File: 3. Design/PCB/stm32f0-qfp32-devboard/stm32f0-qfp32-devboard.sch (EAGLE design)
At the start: 11 parts, among them IC1 STM32F051

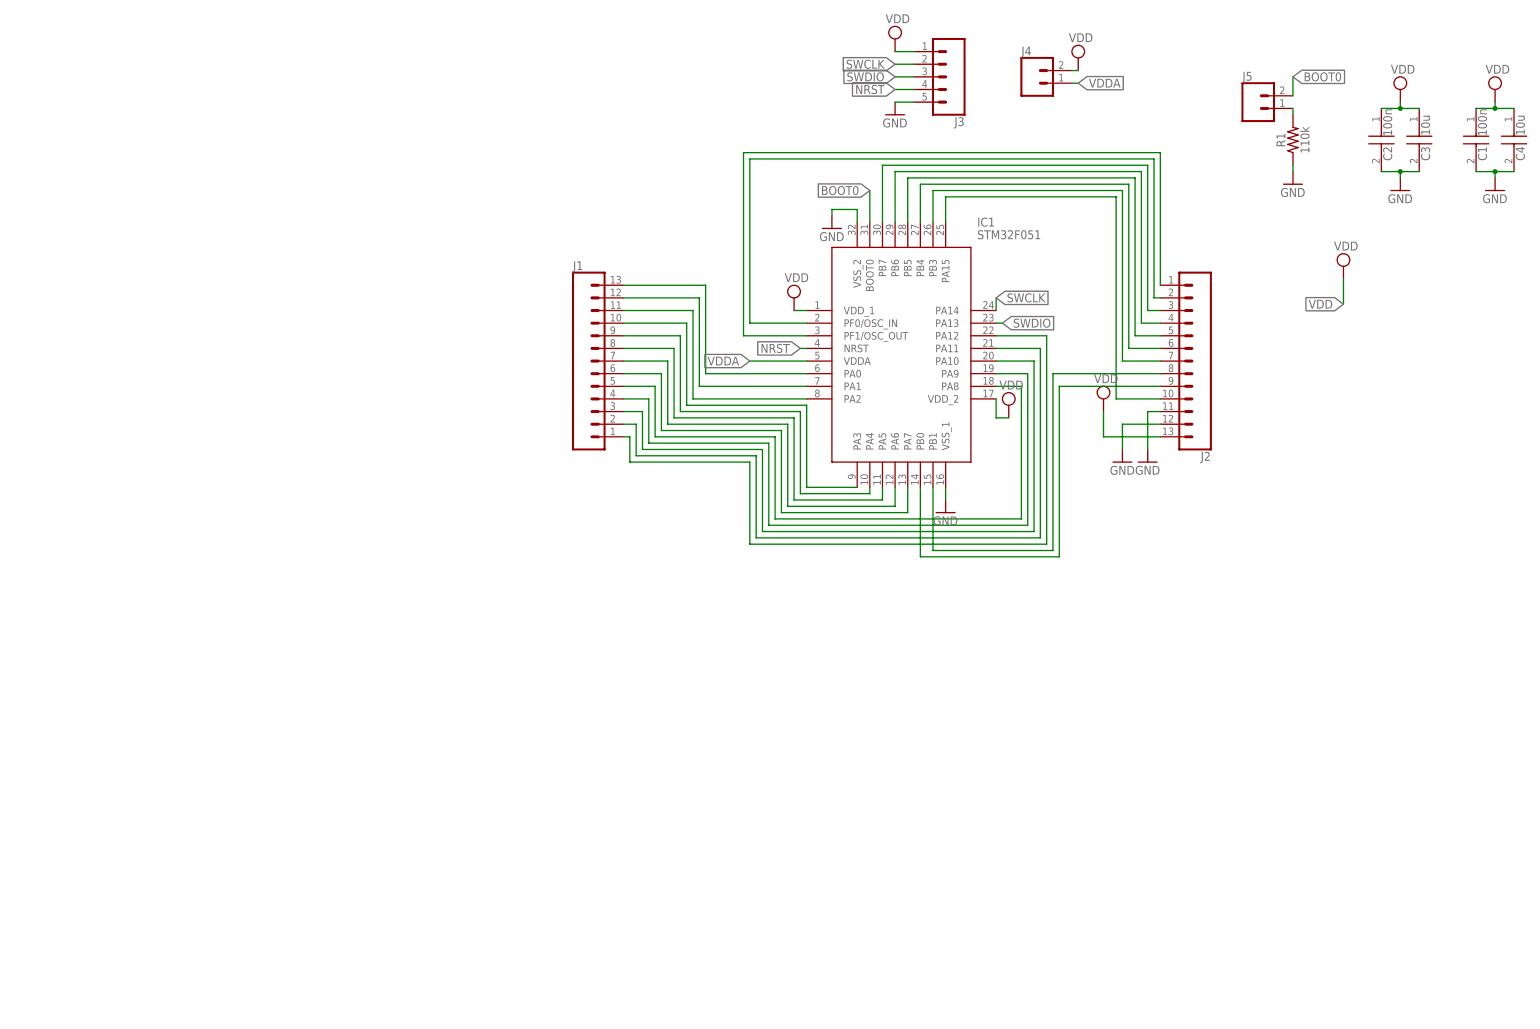
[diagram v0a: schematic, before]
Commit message: ADD: STM32F051 dev board schematic and pcb snapshots
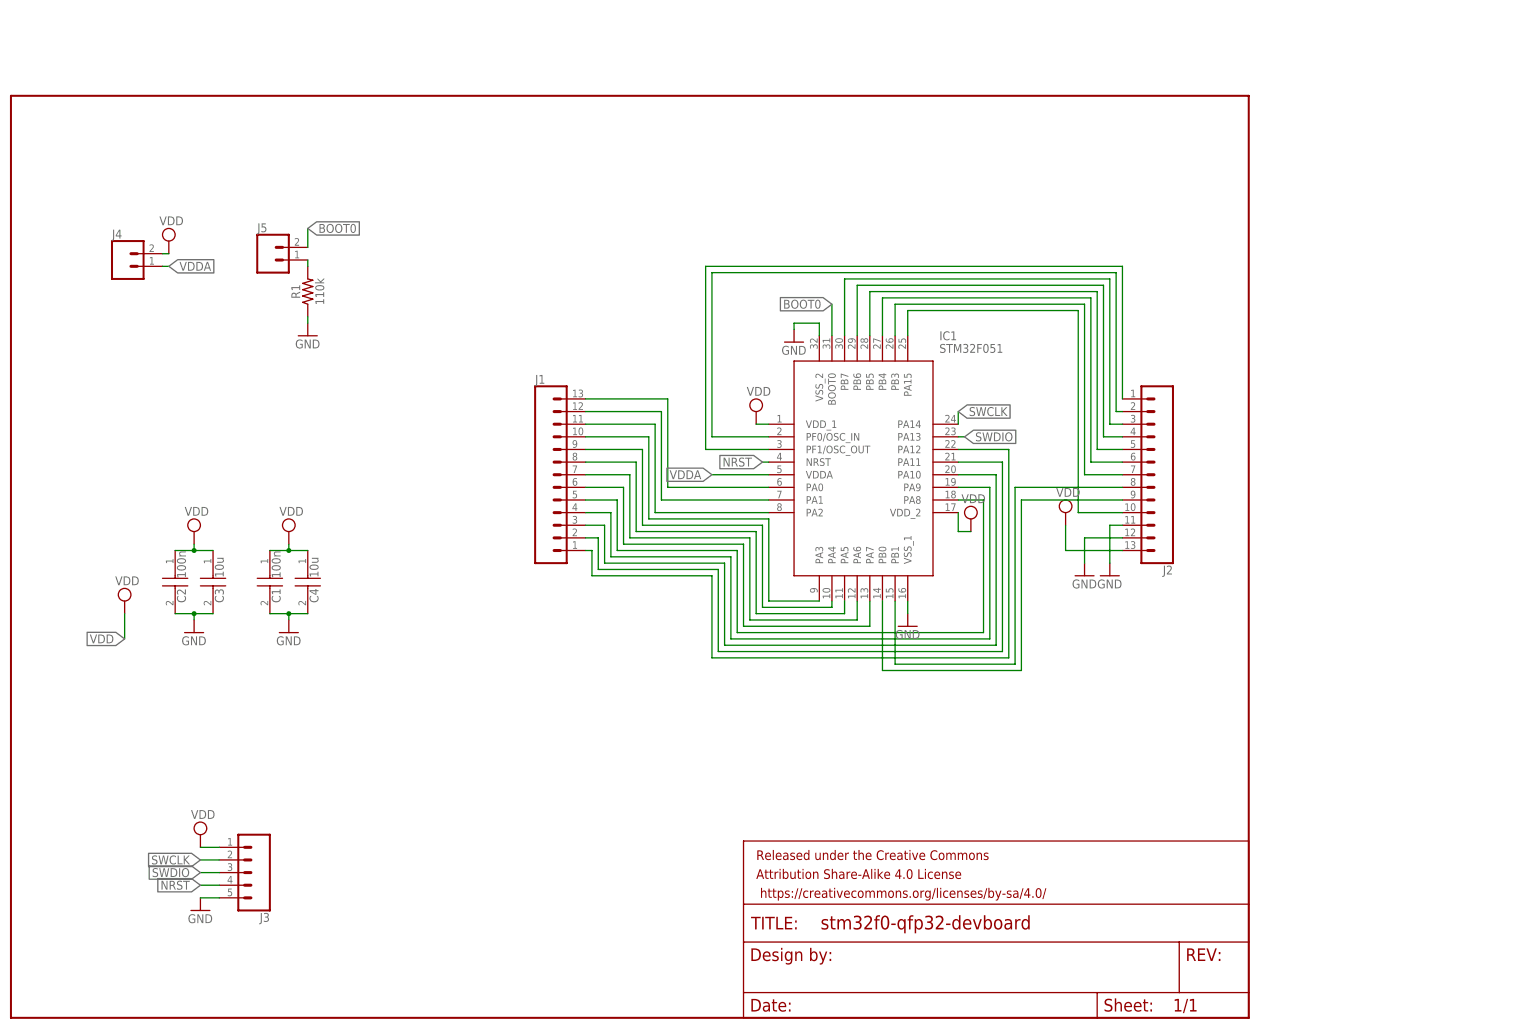
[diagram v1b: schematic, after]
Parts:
- added FRAME2: FRAME-LETTERNO_PACKAGE, SparkFun-Aesthetics:FRAME-LETTERNO_PACKAGE
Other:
- moved on the sheet: C1, C2, C3, C4, IC1, J1, J2, J3, J4, J5, R1
